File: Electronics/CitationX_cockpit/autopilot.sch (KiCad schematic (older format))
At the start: 1 part

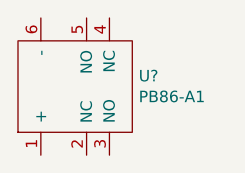
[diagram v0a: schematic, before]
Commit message: Electronics - Misc. works
Continued (and checked board). All connections are probably OK.
Fixed hierarchical pins in APUs (affects all schematics)
Numbered elements for testing schematics
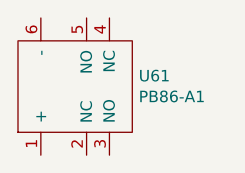
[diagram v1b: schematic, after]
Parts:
- gave numbers to parts that had none: 1
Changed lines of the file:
@@
 $EndDescr
 $Comp
-L adessein:PB86-A1 U?
+L adessein:PB86-A1 U61
 U 1 1 5DBEC5E0
 P 1950 1500
-F 0 "U?" V 1996 922 50  0000 R CNN
+F 0 "U61" V 1996 922 50  0000 R CNN
 F 1 "PB86-A1" V 1905 922 50  0000 R CNN
 F 2 "" H 1950 1500 50  0001 C CNN

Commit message: Electronics - Misc works
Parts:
- removed U61: PB86-A1, symbol adessein:PB86-A1
- added C? (x7): 0.1u, symbol Device:C_Small
- added D? (x8): LED_Small, symbol Device:LED_Small
- added J? (x2): Screw_Terminal_01x10, symbol Connector:Screw_Terminal_01x10
- added R? (x2): 150, symbol Device:R_Small
- added RN? (x3): R_Network08, Resistor_THT:R_Array_SIP9, symbol Device:R_Network08
- added U? (x3): 74HC165, symbol pkl_misc:74HC165
- added U? (x4): 74HC595, symbol 74xx:74HC595
- added U? (x16): PB86-A1, symbol adessein:PB86-A1
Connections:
- new net: U?.10 (SER), U?.9 (QH) (x2)
- new net: U?.14 (SER), U?.9 (QH') (x3)
- new net: RN?.3 (R2), U?.5 (D6)
- new net: RN?.2 (R1), U?.6 (D7)
- new net +3V3: C?.1, C?.1, C?.1, C?.1, C?.1, C?.1, C?.1, RN?.1 (common), RN?.1 (common), RN?.1 (common), U?.10 (~SRCLR), U?.10 (~SRCLR), U?.10 (~SRCLR), U?.10 (~SRCLR), U?.16 (VCC), U?.16 (VCC), U?.16 (VCC), U?.16 (VCC), U?.16 (VCC), U?.16 (VCC), U?.16 (VCC)
- new net ALT: RN?.5 (R4), U?.3 (D4), U?.5 (NO)
- new net ALT_LED: U?.1 (+), U?.6 (QG)
- new net AP: RN?.2 (R1), U?.5 (NO), U?.6 (D7)
- new net APP: RN?.8 (R7), U?.12 (D1), U?.5 (NO)
- new net APP_LED: U?.1 (+), U?.3 (QD)
- new net AP_A_LED: D?.2 (A), U?.1 (QB)
- new net AP_B_LED: D?.2 (A), U?.2 (QC)
- new net ARM_L_LED: J?.4 (Pin_4), U?.15 (QA)
- new net ARM_R_LED: J?.2 (Pin_2), U?.1 (QB)
- new net BANK: RN?.7 (R6), U?.13 (D2), U?.5 (NO)
- new net BANK_LED: U?.1 (+), U?.4 (QE)
- new net BC: RN?.5 (R4), U?.3 (D4), U?.5 (NO)
- new net BC_LED: U?.1 (+), U?.6 (QG)
- new net BOTTLE_L: J?.3 (Pin_3), RN?.7 (R6), U?.13 (D2)
- new net BOTTLE_L_LED: J?.8 (Pin_8), U?.4 (QE)
- new net BOTTLE_R: J?.1 (Pin_1), J?.9 (Pin_9), RN?.4 (R3), U?.4 (D5)
- new net BOTTLE_R_LED: U?.5 (QF)
- new net BOTTLE_T_LED: J?.6 (Pin_6)
- new net CLK: U?.11 (SRCLK), U?.11 (SRCLK), U?.11 (SRCLK), U?.11 (SRCLK), U?.2 (CLK), U?.2 (CLK), U?.2 (CLK)
- new net CO: RN?.9 (R8), U?.11 (D0), U?.5 (NO)
- new net CO_LED: U?.1 (+), U?.2 (QC)
- new net DEPLOY_L_LED: J?.6 (Pin_6), U?.2 (QC)
- new net DEPLOY_R_LED: J?.4 (Pin_4), U?.3 (QD)
- new net ENG_FIRE_L_LED: J?.7 (Pin_7), U?.3 (QD)
- new net ENG_FIRE_R_LED: J?.5 (Pin_5), U?.4 (QE)
- new net FIRE_L: J?.2 (Pin_2), RN?.8 (R7), U?.12 (D1)
- new net FIRE_R: J?.10 (Pin_10), J?.8 (Pin_8), RN?.5 (R4), U?.3 (D4)
- new net FLC: RN?.4 (R3), U?.4 (D5), U?.5 (NO)
- new net FLC_LED: U?.1 (+), U?.7 (QH)
- new net GND: C?.2, C?.2, C?.2, C?.2, C?.2, C?.2, C?.2, R?.2, R?.2, U?.13 (~OE), U?.13 (~OE), U?.13 (~OE), U?.13 (~OE), U?.15 (CLK_INH), U?.15 (CLK_INH), U?.15 (CLK_INH), U?.3 (NO), U?.3 (NO), U?.3 (NO), U?.3 (NO), U?.3 (NO), U?.3 (NO), U?.3 (NO), U?.3 (NO), U?.3 (NO), U?.3 (NO), U?.3 (NO), U?.3 (NO), U?.3 (NO), U?.3 (NO), U?.3 (NO), U?.3 (NO), U?.8 (GND), U?.8 (GND), U?.8 (GND), U?.8 (GND), U?.8 (GND), U?.8 (GND), U?.8 (GND)
- new net HDG: RN?.6 (R5), U?.14 (D3), U?.5 (NO)
- new net HDG_LED: U?.1 (+), U?.5 (QF)
- new net ISR_IN: U?.10 (SER)
- new net ISR_LATCH: U?.1 (SH/~LD), U?.1 (SH/~LD), U?.1 (SH/~LD)
- new net ISR_OUT: U?.9 (QH)
- new net MAV_LED: U?.15 (QA)
- new net MT: RN?.8 (R7), U?.12 (D1), U?.5 (NO)
- new net MT_A_LED: U?.5 (QF)
- new net MT_B_LED: U?.6 (QG)
- new net MT_L_LED: D?.2 (A)
- new net MT_R_LED: D?.2 (A)
- new net NAV: RN?.3 (R2), U?.5 (D6), U?.5 (NO)
- new net NAV_LED: U?.1 (+)
- new net OSR_IN: U?.14 (SER)
- new net OSR_LATCH: U?.12 (RCLK), U?.12 (RCLK), U?.12 (RCLK), U?.12 (RCLK)
- new net OSR_OUT: U?.9 (QH')
- new net PFDS: RN?.7 (R6), U?.13 (D2), U?.5 (NO)
- new net PFD_L_LED: D?.2 (A), U?.7 (QH)
- new net PFD_R_LED: D?.2 (A), U?.15 (QA)
- new net RET_LED: R?.1, U?.6 (-), U?.6 (-), U?.6 (-), U?.6 (-), U?.6 (-), U?.6 (-), U?.6 (-), U?.6 (-), U?.6 (-), U?.6 (-), U?.6 (-), U?.6 (-)
- new net RET_LED_2: D?.1 (K), D?.1 (K), D?.1 (K), D?.1 (K), D?.1 (K), D?.1 (K), D?.1 (K), D?.1 (K), R?.1
- new net SPD: RN?.3 (R2), U?.5 (D6), U?.5 (NO)
- new net SPD_LED: U?.1 (+), U?.15 (QA)
- new net STBY: RN?.4 (R3), U?.4 (D5), U?.5 (NO)
- new net STBY_LED: U?.1 (+), U?.7 (QH)
- new net TR_L: J?.1 (Pin_1), RN?.9 (R8), U?.11 (D0)
- new net TR_R: J?.7 (Pin_7), J?.9 (Pin_9), RN?.6 (R5), U?.14 (D3)
- new net UNLOCK_L_LED: J?.5 (Pin_5), U?.1 (QB), U?.2 (QC)
- new net UNLOCK_R_LED: J?.3 (Pin_3)
- new net VNAV: RN?.2 (R1), U?.5 (NO), U?.6 (D7)
- new net VNAV_LED: U?.1 (+), U?.1 (QB)
- new net VS: RN?.6 (R5), U?.14 (D3), U?.5 (NO)
- new net VS_LED: U?.1 (+), U?.5 (QF)
- new net YD: RN?.9 (R8), U?.11 (D0), U?.5 (NO)
- new net YD_A_LED: D?.2 (A), U?.3 (QD)
- new net YD_B_LED: D?.2 (A), U?.4 (QE)
- no-connect marks 0 -> 3

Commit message: Electronics - Added transistor array ULN2803A to LEDS in autopilot
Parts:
- added U? (x4): ULN2803A, symbol Transistor_Array:ULN2803A
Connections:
- net ALT_LED: now also U?.12 (O7); no longer U?.6 (QG)
- net APP_LED: now also U?.15 (O4); no longer U?.3 (QD)
- net AP_A_LED: now also U?.17 (O2); no longer U?.1 (QB)
- net AP_B_LED: now also U?.16 (O3); no longer U?.2 (QC)
- net ARM_L_LED: now also U?.18 (O1); no longer U?.15 (QA)
- net ARM_R_LED: now also U?.18 (O1); no longer U?.1 (QB)
- net BANK_LED: now also U?.14 (O5); no longer U?.4 (QE)
- net BC_LED: now also U?.12 (O7); no longer U?.6 (QG)
- net BOTTLE_L_LED: now also U?.14 (O5); no longer U?.4 (QE)
- net BOTTLE_R_LED: now also U?.14 (O5); no longer U?.5 (QF)
- net CO_LED: now also U?.16 (O3); no longer U?.2 (QC)
- net DEPLOY_L_LED: now also U?.16 (O3); no longer U?.2 (QC)
- net DEPLOY_R_LED: now also U?.16 (O3); no longer U?.3 (QD)
- net ENG_FIRE_L_LED: now also U?.15 (O4); no longer U?.3 (QD)
- net ENG_FIRE_R_LED: now also U?.15 (O4); no longer U?.4 (QE)
- net FLC_LED: now also U?.11 (O8); no longer U?.7 (QH)
- net GND: now also U?.9 (GND), U?.9 (GND), U?.9 (GND), U?.9 (GND)
- net HDG_LED: now also U?.13 (O6); no longer U?.5 (QF)
- net MAV_LED: now also U?.18 (O1); no longer U?.15 (QA)
- net MT_A_LED: now also U?.13 (O6); no longer U?.5 (QF)
- net MT_B_LED: now also U?.12 (O7); no longer U?.6 (QG)
- net PFD_L_LED: now also U?.11 (O8); no longer U?.7 (QH)
- net PFD_R_LED: now also U?.10 (COM); no longer U?.15 (QA)
- net SPD_LED: now also U?.18 (O1); no longer U?.15 (QA)
- net STBY_LED: now also U?.11 (O8); no longer U?.7 (QH)
- net UNLOCK_L_LED: now also U?.17 (O2), U?.17 (O2); no longer U?.1 (QB), U?.2 (QC)
- net VNAV_LED: now also U?.17 (O2); no longer U?.1 (QB)
- net VS_LED: now also U?.13 (O6); no longer U?.5 (QF)
- net YD_A_LED: now also U?.15 (O4); no longer U?.3 (QD)
- net YD_B_LED: now also U?.14 (O5); no longer U?.4 (QE)
- net at U?.6 (QG): now also U?.7 (I7)
- net at U?.7 (QH): now also U?.8 (I8)
- new net: U?.1 (QB), U?.2 (I2) (x4)
- new net: U?.1 (I1), U?.15 (QA) (x4)
- new net: U?.2 (QC), U?.3 (I3) (x4)
- new net: U?.3 (QD), U?.4 (I4) (x4)
- new net: U?.4 (QE), U?.5 (I5) (x4)
- new net: U?.5 (QF), U?.6 (I6) (x4)
- new net: U?.6 (QG), U?.7 (I7) (x3)
- new net: U?.7 (QH), U?.8 (I8) (x3)
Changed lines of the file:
@@
 	0    -1   -1   0
 $EndComp
-Text Label 5800 1850 0    50   ~ 0
+Text Label 6050 1850 0    50   ~ 0
 HDG_LED
-Text Label 5800 1950 0    50   ~ 0
+Text Label 6050 1950 0    50   ~ 0
 ALT_LED
-Text Label 5800 2050 0    50   ~ 0
+Text Label 6050 2050 0    50   ~ 0
 FLC_LED
 Wire Wire Line
 	900  2050 850  2050
-Text Label 5800 3350 0    50   ~ 0
+Text Label 6050 3350 0    50   ~ 0
 MAV_LED
-Text Label 5800 3450 0    50   ~ 0
+Text Label 6050 3450 0    50   ~ 0
 VNAV_LED
-Text Label 5800 3550 0    50   ~ 0
+Text Label 6050 3550 0    50   ~ 0
 CO_LED
-Text Label 5800 3650 0    50   ~ 0
+Text Label 6050 3650 0    50   ~ 0
 APP_LED
-Text Label 5800 3750 0    50   ~ 0
+Text Label 6050 3750 0    50   ~ 0
 BANK_LED
-Text Label 5800 3850 0    50   ~ 0
+Text Label 6050 3850 0    50   ~ 0
 VS_LED
 Text GLabel 1850 2250 0    50   Input ~ 0
@@
 Text GLabel 4450 1550 0    50   Input ~ 0
 CLK
-Text Label 5800 3950 0    50   ~ 0
+Text Label 6050 3950 0    50   ~ 0
 BC_LED
-Text Label 5800 4050 0    50   ~ 0
+Text Label 6050 4050 0    50   ~ 0
 STBY_LED
-Text Label 5800 5450 0    50   ~ 0
+Text Label 6050 5450 0    50   ~ 0
 AP_A_LED
-Text Label 5800 5550 0    50   ~ 0
+Text Label 6050 5550 0    50   ~ 0
 AP_B_LED
-Text Label 5800 5650 0    50   ~ 0
+Text Label 6050 5650 0    50   ~ 0
 YD_A_LED
-Text Label 5800 5750 0    50   ~ 0
+Text Label 6050 5750 0    50   ~ 0
 YD_B_LED
-Text Label 5800 5350 0    50   ~ 0
+Text Label 6050 5350 0    50   ~ 0
 SPD_LED
 Text GLabel 1850 3950 0    50   Input ~ 0
@@
 	0    -1   -1   0
 $EndComp
-Text Label 5800 5850 0    50   ~ 0
+Text Label 6050 5850 0    50   ~ 0
 MT_A_LED
-Text Label 5800 5950 0    50   ~ 0
+Text Label 6050 5950 0    50   ~ 0
 MT_B_LED
 Text GLabel 1850 5650 0    50   Input ~ 0
@@
 Text Label 1300 1550 0    50   ~ 0
 BOTTLE_L
-Wire Wire Line
-	5800 1350 5250 1350
-Wire Wire Line
-	5250 1450 5800 1450
-Wire Wire Line
-	5800 1550 5250 1550
-Wire Wire Line
-	5250 1650 5800 1650
-Wire Wire Line
-	5800 1750 5250 1750
-Wire Wire Line
-	5250 1850 5800 1850
-Wire Wire Line
-	5800 1950 5250 1950
-Wire Wire Line
-	5250 2050 5800 2050
-Wire Wire Line
-	5800 3350 5250 3350
-Wire Wire Line
-	5250 3450 5800 3450
-Wire Wire Line
-	5800 3550 5250 3550
-Wire Wire Line
-	5250 3650 5800 3650
-Wire Wire Line
-	5800 3750 5250 3750
-Wire Wire Line
-	5250 3850 5800 3850
-Wire Wire Line
-	5800 3950 5250 3950
-Wire Wire Line
-	5250 4050 5800 4050
-Text Label 5800 1350 0    50   ~ 0
+Text Label 6050 1350 0    50   ~ 0
 ARM_L_LED
-Text Label 5800 1450 0    50   ~ 0
+Text Label 6050 1450 0    50   ~ 0
 UNLOCK_L_LED
-Text Label 5800 1550 0    50   ~ 0
+Text Label 6050 1550 0    50   ~ 0
 DEPLOY_L_LED
-Text Label 5800 1650 0    50   ~ 0
+Text Label 6050 1650 0    50   ~ 0
 ENG_FIRE_L_LED
-Text Label 5800 1750 0    50   ~ 0
+Text Label 6050 1750 0    50   ~ 0
 BOTTLE_L_LED
-Text Label 5800 7350 0    50   ~ 0
+Text Label 6600 7250 0    50   ~ 0
 PFD_R_LED
-Text Label 5800 6050 0    50   ~ 0
+Text Label 6050 6050 0    50   ~ 0
 PFD_L_LED
-Wire Wire Line
-	5800 5350 5250 5350
-Wire Wire Line
-	5250 5450 5800 5450
-Wire Wire Line
-	5800 5550 5250 5550
-Wire Wire Line
-	5250 5650 5800 5650
-Wire Wire Line
-	5800 5750 5250 5750
-Wire Wire Line
-	5250 5850 5800 5850
-Wire Wire Line
-	5800 5950 5250 5950
-Wire Wire Line
-	5250 6050 5800 6050
 $Comp
 L Device:C_Small C?
@@
 Wire Wire Line
 	5250 6700 5250 6250
-Wire Wire Line
-	5800 7350 5250 7350
-Wire Wire Line
-	5250 7450 5800 7450
-Wire Wire Line
-	5800 7550 5250 7550
-Wire Wire Line
-	5250 7650 5800 7650
-Wire Wire Line
-	5800 7750 5250 7750
-Wire Wire Line
-	5250 7850 5800 7850
-Wire Wire Line
-	5800 7950 5250 7950
-Wire Wire Line
-	5250 8050 5800 8050
-Text Label 5800 7450 0    50   ~ 0
+Text Label 6600 7350 0    50   ~ 0
 ARM_R_LED
-Text Label 5800 7550 0    50   ~ 0
+Text Label 6600 7450 0    50   ~ 0
 UNLOCK_L_LED
-Text Label 5800 7650 0    50   ~ 0
+Text Label 6600 7550 0    50   ~ 0
 DEPLOY_R_LED
-Text Label 5800 7750 0    50   ~ 0
+Text Label 6600 7650 0    50   ~ 0
 ENG_FIRE_R_LED
-Text Label 5800 7850 0    50   ~ 0
+Text Label 6600 7750 0    50   ~ 0
 BOTTLE_R_LED
 $Comp
@@
 Text HLabel 3050 5450 2    50   Output ~ 0
 ISR_OUT
+$Comp
+L Transistor_Array:ULN2803A U?
+U 1 1 5E5190F9
+P 6200 7550
+F 0 "U?" H 6200 8117 50  0000 C CNN
+F 1 "ULN2803A" H 6200 8026 50  0000 C CNN
+F 2 "" H 6250 6900 50  0001 L CNN
+F 3 "http://www.ti.com/lit/ds/symlink/uln2803a.pdf" H 6300 7350 50  0001 C CNN
+	1    6200 7550
+	1    0    0    -1
+$EndComp
+$Comp
+L power:GND #PWR?
+U 1 1 5E51910F
+P 6200 8250
+AR Path="/5DB5DCD1/5E51910F" Ref="#PWR?"  Part="1"
+AR Path="/5DC174D4/5E51910F" Ref="#PWR?"  Part="1"
+AR Path="/5DBF6FEB/5E51910F" Ref="#PWR?"  Part="1"
+F 0 "#PWR?" H 6200 8000 50  0001 C CNN
+F 1 "GND" H 6205 8077 50  0000 C CNN
+F 2 "" H 6200 8250 50  0001 C CNN
+F 3 "" H 6200 8250 50  0001 C CNN
+	1    6200 8250
+	0    1    1    0
+$EndComp
+$Comp
+L Transistor_Array:ULN2803A U?
+U 1 1 5E53E8B4
+P 5650 1550
+F 0 "U?" H 5650 2117 50  0000 C CNN
+F 1 "ULN2803A" H 5650 2026 50  0000 C CNN
+F 2 "" H 5700 900 50  0001 L CNN
+F 3 "http://www.ti.com/lit/ds/symlink/uln2803a.pdf" H 5750 1350 50  0001 C CNN
+	1    5650 1550
+	1    0    0    -1
+$EndComp
+$Comp
+L power:GND #PWR?
+U 1 1 5E53E8BA
+P 5650 2250
+AR Path="/5DB5DCD1/5E53E8BA" Ref="#PWR?"  Part="1"
+AR Path="/5DC174D4/5E53E8BA" Ref="#PWR?"  Part="1"
+AR Path="/5DBF6FEB/5E53E8BA" Ref="#PWR?"  Part="1"
+F 0 "#PWR?" H 5650 2000 50  0001 C CNN
+F 1 "GND" H 5655 2077 50  0000 C CNN
+F 2 "" H 5650 2250 50  0001 C CNN
+F 3 "" H 5650 2250 50  0001 C CNN
+	1    5650 2250
+	0    1    1    0
+$EndComp
+$Comp
+L Transistor_Array:ULN2803A U?
+U 1 1 5E545A18
+P 5650 3550
+F 0 "U?" H 5650 4117 50  0000 C CNN
+F 1 "ULN2803A" H 5650 4026 50  0000 C CNN
+F 2 "" H 5700 2900 50  0001 L CNN
+F 3 "http://www.ti.com/lit/ds/symlink/uln2803a.pdf" H 5750 3350 50  0001 C CNN
+	1    5650 3550
+	1    0    0    -1
+$EndComp
+$Comp
+L power:GND #PWR?
+U 1 1 5E545A1E
+P 5650 4250
+AR Path="/5DB5DCD1/5E545A1E" Ref="#PWR?"  Part="1"
+AR Path="/5DC174D4/5E545A1E" Ref="#PWR?"  Part="1"
+AR Path="/5DBF6FEB/5E545A1E" Ref="#PWR?"  Part="1"
+F 0 "#PWR?" H 5650 4000 50  0001 C CNN
+F 1 "GND" H 5655 4077 50  0000 C CNN
+F 2 "" H 5650 4250 50  0001 C CNN
+F 3 "" H 5650 4250 50  0001 C CNN
+	1    5650 4250
+	0    1    1    0
+$EndComp
+$Comp
+L Transistor_Array:ULN2803A U?
+U 1 1 5E555812
+P 5650 5550
+F 0 "U?" H 5650 6117 50  0000 C CNN
+F 1 "ULN2803A" H 5650 6026 50  0000 C CNN
+F 2 "" H 5700 4900 50  0001 L CNN
+F 3 "http://www.ti.com/lit/ds/symlink/uln2803a.pdf" H 5750 5350 50  0001 C CNN
+	1    5650 5550
+	1    0    0    -1
+$EndComp
+$Comp
+L power:GND #PWR?
+U 1 1 5E555818
+P 5650 6250
+AR Path="/5DB5DCD1/5E555818" Ref="#PWR?"  Part="1"
+AR Path="/5DC174D4/5E555818" Ref="#PWR?"  Part="1"
+AR Path="/5DBF6FEB/5E555818" Ref="#PWR?"  Part="1"
+F 0 "#PWR?" H 5650 6000 50  0001 C CNN
+F 1 "GND" H 5655 6077 50  0000 C CNN
+F 2 "" H 5650 6250 50  0001 C CNN
+F 3 "" H 5650 6250 50  0001 C CNN
+	1    5650 6250
+	0    1    1    0
+$EndComp
+Wire Wire Line
+	5250 8050 5800 8050
+Wire Wire Line
+	5800 7950 5250 7950
+Wire Wire Line
+	5250 7850 5800 7850
+Wire Wire Line
+	5800 7750 5250 7750
+Wire Wire Line
+	5250 7650 5800 7650
+Wire Wire Line
+	5800 7550 5250 7550
+Wire Wire Line
+	5250 7450 5800 7450
+Wire Wire Line
+	5800 7350 5250 7350
 $EndSCHEMATC
